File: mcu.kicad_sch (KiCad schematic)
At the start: 47 parts, among them J1 USB_C_Receptacle_USB2.0_16P, J4 Conn_01x03_Pin, J5 Conn_01x03_Pin, J6 Conn_02x04_Odd_Even, J7 AudioJack2_Ground_Switch, SW4 RotaryEncoder_Switch, SW5 RESET, SW6 BOOTSEL, U1 RP2040, U5 W25Q64JVSSIQ, U6 ADS1015IDGS, Y1 XYDBPCNANF-12MHZ

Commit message: stm32g0
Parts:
- removed Brd1: SSD1306, SSD1306:128x64OLED, symbol SSD1306-128x64_OLED:SSD1306
- removed C11, C12: 12pF, Capacitor_SMD:C_0603_1608Metric, symbol Device:C_Small
- removed C13, C14, C15, C16, C17, C19, C20, C26, C5: 0.1uF, Capacitor_SMD:C_0603_1608Metric, symbol Device:C_Small
- removed C18, C21: 1uF, Capacitor_SMD:C_0603_1608Metric, symbol Device:C_Small
- removed J4: Conn_01x03_Pin, Connector_JST:JST_SH_SM03B-SRSS-TB_1x03-1MP_P1.00mm_Horizontal, symbol Connector:Conn_01x03_Pin
- removed J5: Conn_01x03_Pin, Connector_PinHeader_2.54mm:PinHeader_1x03_P2.54mm_Vertical, symbol Connector:Conn_01x03_Pin
- removed J6: Conn_02x04_Odd_Even, Connector_PinHeader_2.54mm:PinHeader_2x04_P2.54mm_Vertical, symbol Connector_Generic:Conn_02x04_Odd_Even
- removed R12, R15, R16, R17: 100K 1%, Resistor_SMD:R_0603_1608Metric, symbol Device:R_Small
- removed R19, R23: 10K, Resistor_SMD:R_0603_1608Metric, symbol Device:R_Small
- removed R20, R21: 22, Resistor_SMD:R_0603_1608Metric, symbol Device:R_Small
- removed R22, R27: 1K, Resistor_SMD:R_0603_1608Metric, symbol Device:R_Small
- removed R47, R48: 100, Resistor_SMD:R_0603_1608Metric, symbol Device:R_US
- removed SW5: RESET, Button_Switch_SMD:SW_Push_1P1T_NO_E-Switch_TL3301NxxxxxG, symbol Switch:SW_Push
- removed SW6: BOOTSEL, Button_Switch_SMD:SW_Push_1P1T_NO_E-Switch_TL3301NxxxxxG, symbol Switch:SW_Push
- removed U1: RP2040, Package_DFN_QFN:QFN-56-1EP_7x7mm_P0.4mm_EP3.2x3.2mm, symbol MCU_RaspberryPi:RP2040
- removed U5: W25Q64JVSSIQ, Package_SO:SOIC-8_5.3x5.3mm_P1.27mm, symbol Memory_Flash_Extra:GD25Q32C
- removed U6: ADS1015IDGS, Package_SO:TSSOP-10_3x3mm_P0.5mm, symbol Analog_ADC:ADS1015IDGS
- removed Y1: XYDBPCNANF-12MHZ, Crystal:Crystal_SMD_3225-4Pin_3.2x2.5mm, symbol Device:Crystal_GND24_Small
- added C28, C37, C39, C47, C48, C49: 100nF, Capacitor_SMD:C_0603_1608Metric, symbol Device:C_Small
- added C29, C30, C42, C43, C44: 4.7uF, Capacitor_SMD:C_0603_1608Metric_Pad1.08x0.95mm_HandSolder, symbol Device:C
- added C45, C46: 100nF, Capacitor_SMD:C_0603_1608Metric, symbol Device:C
- added C50: 1uF, Capacitor_SMD:C_0603_1608Metric, symbol Device:C_Small
- added D15, D16, D17, D18, D19: 1N5819WS, Diode_SMD:D_SOD-323, symbol Diode:1N5819WS
- added D20, D21: SMF18A, Diode_SMD:D_SMF, symbol Diode:SMF18A
- added J2: Conn_01x04_Pin, Connector_PinSocket_2.54mm:PinSocket_1x04_P2.54mm_Vertical, symbol Connector:Conn_01x04_Pin
- added J3: AudioJack2_Ground_Switch, Connector_Audio:Jack_3.5mm_CUI_SJ1-3525N_Horizontal, symbol Connector_Audio:AudioJack3_SwitchTR
- added J4: AudioJack2_Ground_Switch, 2.5mm:Jack_2.5mm_PJ242_6P_12x6.2x4mm_Horizontal, symbol Connector_Audio:AudioJack3_SwitchTR
- added J5, J6: Conn_01x04_Pin, Connector_PinHeader_2.54mm:PinHeader_1x04_P2.54mm_Vertical, symbol Connector:Conn_01x04_Pin
- added Q2: BSS138, Package_TO_SOT_SMD:SOT-23, symbol Transistor_FET:BSS138
- added R29, R30: 22R, Resistor_SMD:R_0603_1608Metric, symbol Device:R_Small
- added R33, R37, R51: 100R, Resistor_SMD:R_0603_1608Metric, symbol Device:R
- added R34, R35: 100K, Resistor_SMD:R_0603_1608Metric_Pad0.98x0.95mm_HandSolder, symbol Device:R
- added R36, R38, R50: 10K, Resistor_SMD:R_0603_1608Metric_Pad0.98x0.95mm_HandSolder, symbol Device:R
- added R39, R43: 680R, Resistor_SMD:R_0603_1608Metric_Pad0.98x0.95mm_HandSolder, symbol Device:R
- added R40, R44: 470K 1%, Resistor_SMD:R_0603_1608Metric, symbol Device:R_Small
- added R41, R45, R46, R47, R48, R49: 100K 1%, Resistor_SMD:R_0603_1608Metric, symbol Device:R_Small
- added R42: 470R, Resistor_SMD:R_0603_1608Metric_Pad0.98x0.95mm_HandSolder, symbol Device:R
- added SW7, SW8, SW9: TRIGGER, Button_Switch_SMD:YZA-032-5.0W, symbol Switch:SW_Push
- added U1: STM32G0B1RETx, Package_QFP:LQFP-64_10x10mm_P0.5mm, symbol MCU_ST_STM32G0:STM32G0B1RETx
- added U8: LM358B, Package_SO:SOIC-8_3.9x4.9mm_P1.27mm, symbol Amplifier_Operational:LM358
- D10, D11, D14, D9: footprint Diode_SMD:D_0201_0603Metric -> Diode_SMD:D_0402_1005Metric; LCSC C52994072 -> C316049
- R10, R9: LCSC (none) -> C23186
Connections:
- net +3.3V: now also C47.1, C48.1, C49.1, C50.1, D15.2 (A), J2.4 (Pin_4), J6.3 (Pin_3), SW9.2, U1.6 (VBAT), U1.7 (VREF+), U1.8 (VDD)
- net +5V: now also R47.1
- net +BATT: now also C28.1, R34.1, R49.1, U8.8 (V+)
- net BATT_SENSE: now also R48.1, R49.2, U1.28 (PB1)
- net BTN_OK: now also U1.54 (PD4)
- net BUZZER1: now also U1.1 (PC11)
- net BUZZER2: now also U1.2 (PC12)
- net CHARGE_PUMP_OSC0: now also R51.1, U1.15 (PC2)
- net CHARGE_PUMP_OSC1: now also R33.1, U1.14 (PC1)
- net CURRENT_SENSE: now also Q2.2 (S), R38.2, R43.2, U1.17 (PA0)
- net D+: now also R30.2
- net D-: now also R29.2
- net GND: now also C28.2, C37.1, C39.1, C44.2, C45.2, C46.2, C47.2, C48.2, C49.2, C50.2, D20.2 (A2), D21.2 (A2), J2.3 (Pin_3), J5.4 (Pin_4), J6.4 (Pin_4), R35.2, R36.1, R41.2, R43.1, R45.2, R46.2, R48.2, SW7.1, SW8.2, U1.9 (VSS), U8.4 (V-)
- net R1: now also SW4.B, U1.53 (PD3); no longer SW4.A
- net R2: now also SW4.A, U1.52 (PD2); no longer SW4.B
- net SWCLK: now also J2.2 (Pin_2), SW9.1, U1.46 (PA14)
- net SWDIO: now also J2.1 (Pin_1), U1.45 (PA13)
- net USB_SENSE: now also R46.1, R47.2, U1.48 (PC8)
- net ~{RESET}: now also C37.2, SW8.1, U1.12 (PF2)
- net FOOT_PEDAL renamed TRIGGER
- net TRIGGER: now also C39.2, SW7.2, U1.29 (PB2)
- new net: R36.2, R50.1, U8.3 (+)
- new net: Q2.1 (G), R39.1
- new net: C43.1, D18.1 (K), D19.2 (A)
- new net: C30.2, C43.2, R51.2
- new net: R34.2, R35.1, U8.5 (+)
- new net: C44.1, D19.1 (K), R37.1
- new net: C29.1, D15.1 (K), D16.2 (A)
- new net: C29.2, C42.2, R33.2
- new net: R38.1, U8.2 (-)
- new net: C30.1, D16.1 (K), D17.2 (A)
- new net: C42.1, D17.1 (K), D18.2 (A)
- new net: R29.1, U1.43 (PA9/PA11)
- new net: R30.1, U1.44 (PA10/PA12)
- new net: R39.2, U8.1
- new net: U8.6 (-), U8.7
- new net: J3.TN, R42.1
- new net BODY_ELECTRODE: D20.1 (A1), J4.R, J4.S, J4.T, R37.2, R44.1
- new net DAC_OUT1: R50.2, U1.21 (PA4)
- new net FOLLICLE_ELECTRODE: D21.1 (A1), J3.R, J3.S, Q2.3 (D), R40.1, R42.2
- new net I2C2_SCL: J6.2 (Pin_2), U1.30 (PB10)
- new net I2C2_SDA: J6.1 (Pin_1), U1.31 (PB11)
- new net OUTPUT_HIGH: C46.1, R44.2, R45.1, U1.32 (PB12)
- new net OUTPUT_LOW: C45.1, R40.2, R41.1, U1.22 (PA5)
- new net PA15: J5.1 (Pin_1), U1.47 (PA15)
- new net PC9: J5.2 (Pin_2), U1.49 (PC9)
- new net PD0: J5.3 (Pin_3), U1.50 (PD0)
- no-connect marks 16 -> 6
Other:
- note added: "Current 0mA-2.426mA w/ 0.6uA stepping"
- note added: "Drive at 1kHz square; alternative phase"
- note added: "Foot pedal can be used or on device button"
- note added: "R for self-testing"
- note removed: "12MHz"
- note removed: "Address 0b1001000"
- note removed: "PWM3 A/B"
- note removed: "PWM7 A/B"
- moved on the sheet: BZ1, C24, D10, D11, D14, D9, J1, J7, R10, R9, SW4

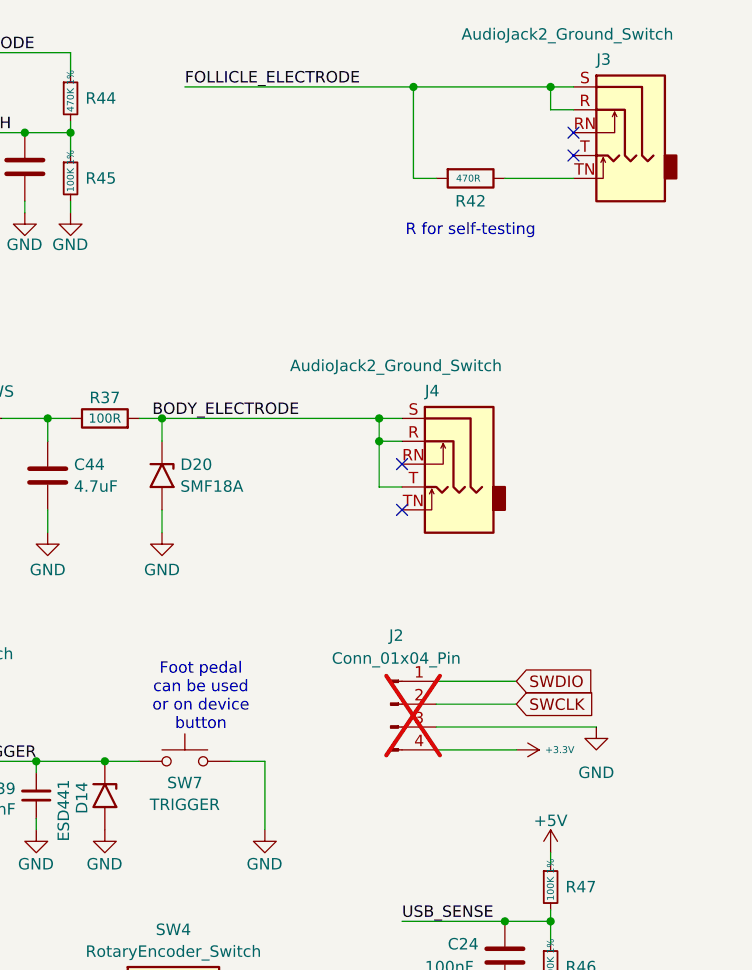
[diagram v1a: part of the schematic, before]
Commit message: fixed some shorts and bad dummy load configuration
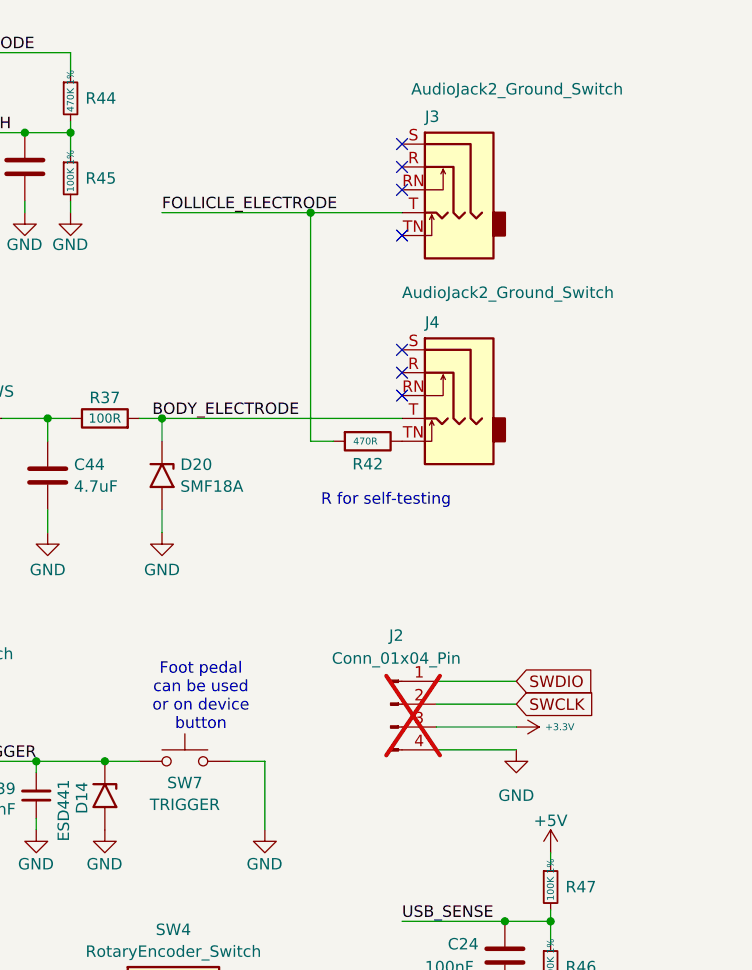
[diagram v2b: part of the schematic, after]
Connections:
- net +3.3V: now also J2.3 (Pin_3); no longer J2.4 (Pin_4)
- net BODY_ELECTRODE: no longer J4.R, J4.S
- net FOLLICLE_ELECTRODE: now also J3.T; no longer J3.R, J3.S
- net GND: now also J2.4 (Pin_4); no longer J2.3 (Pin_3)
- net at J4.TN: now also R42.1
- net at J3.TN: no longer R42.1
- no-connect marks 6 -> 9
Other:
- moved on the sheet: J3, J4, R42

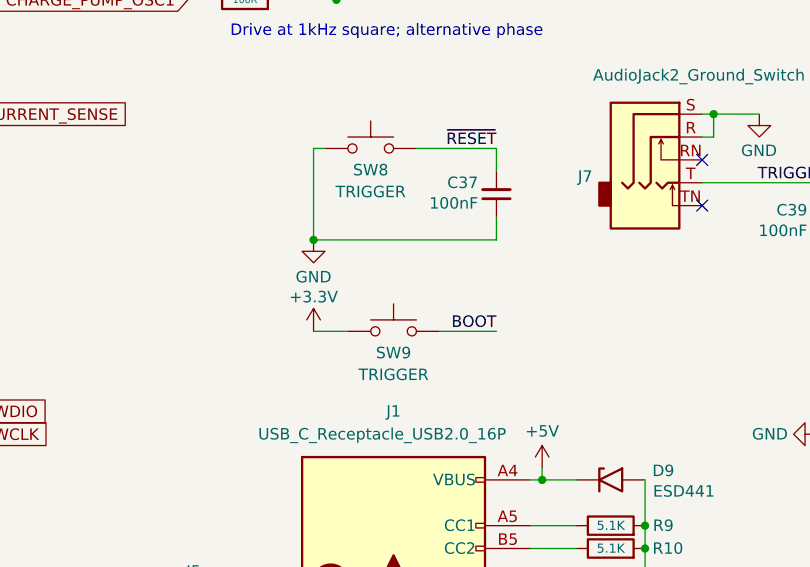
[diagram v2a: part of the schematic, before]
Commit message: Fix C37 LCSC code, changed buttons to C720477
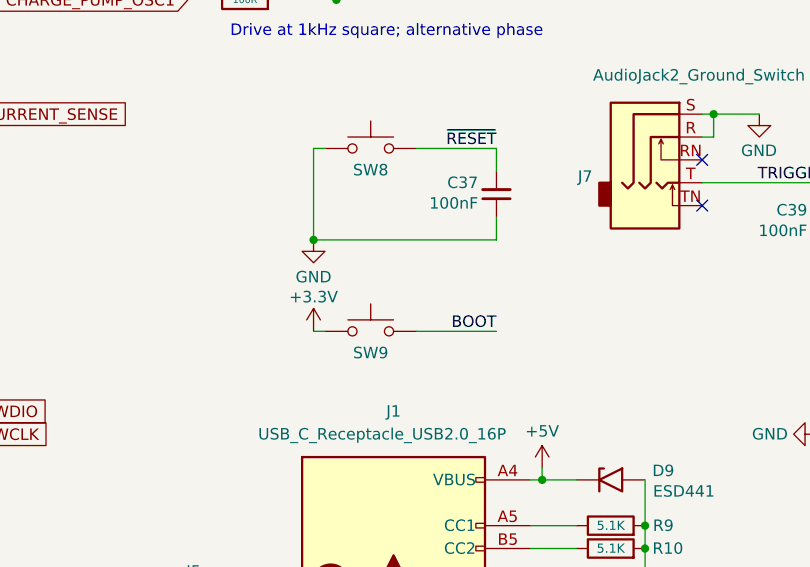
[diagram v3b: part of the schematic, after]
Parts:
- C37: LCSC C15849 -> C14663
- SW8: value TRIGGER -> RST; footprint Button_Switch_SMD:YZA-032-5.0W -> Button_Switch_SMD:SW_SPST_TS-1088-xR025
- SW9: value TRIGGER -> BOOT; footprint Button_Switch_SMD:YZA-032-5.0W -> Button_Switch_SMD:SW_SPST_TS-1088-xR025
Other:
- moved on the sheet: SW9

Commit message: Removed USB resistors, shuffled breakout pins to tidy up a tad
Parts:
- removed R29, R30: 22R, Resistor_SMD:R_0603_1608Metric, symbol Device:R_Small
- SW7: footprint Button_Switch_SMD:YZA-032-5.0W -> Button_Switch_SMD:SW_SPST_TS-1088-xR025; LCSC C49108628 -> C720477
- SW8, SW9: LCSC C49108628 -> C720477
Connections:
- net D+: now also U1.44 (PA10/PA12)
- net D-: now also U1.43 (PA9/PA11)
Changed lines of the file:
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@@
 	(wire
 		(pts
-			(xy 107.95 119.38) (xy 114.3 119.38)
-		)
-		(stroke
-			(width 0)
-			(type default)
-		)
-	)
-	(wire
-		(pts
 			(xy 152.4 60.96) (xy 154.94 60.96)
 		)
@@
 	(wire
 		(pts
-			(xy 99.06 114.3) (xy 102.87 114.3)
+			(xy 99.06 114.3) (xy 114.3 114.3)
 		)
 		(stroke
@@
 	(wire
 		(pts
-			(xy 34.29 101.6) (xy 43.18 101.6)
+			(xy 27.94 101.6) (xy 43.18 101.6)
 		)
 		(stroke
@@
 	(wire
 		(pts
-			(xy 99.06 119.38) (xy 102.87 119.38)
+			(xy 99.06 119.38) (xy 114.3 119.38)
 		)
 		(stroke
@@
 	(wire
 		(pts
-			(xy 107.95 114.3) (xy 114.3 114.3)
-		)
-		(stroke
-			(width 0)
-			(type default)
-		)
-	)
-	(wire
-		(pts
 			(xy 125.73 44.45) (xy 125.73 46.99)
 		)
@@
 	)
 	(label "~{RESET}"
-		(at 34.29 101.6 0)
+		(at 27.94 101.6 0)
 		(effects
 			(font
@@
 			)
 		)
-		(property "LCSC" "C49108628"
+		(property "LCSC" "C720477"
 			(at 158.75 95.25 0)
 			(hide yes)
@@
 			)
 		)
-		(property "Footprint" "Button_Switch_SMD:YZA-032-5.0W"
+		(property "Footprint" "Button_Switch_SMD:SW_SPST_TS-1088-xR025"
 			(at 226.06 93.98 0)
 			(hide yes)
@@
 			)
 		)
-		(property "LCSC" "C49108628"
+		(property "LCSC" "C720477"
 			(at 226.06 99.06 0)
 			(hide yes)
@@
 			)
 		)
-		(property "LCSC" "C49108628"
+		(property "LCSC" "C720477"
 			(at 158.75 115.57 0)
 			(hide yes)
@@
 	(symbol
 		(lib_id "Device:R_Small")
-		(at 105.41 119.38 90)
-		(mirror x)
-		(unit 1)
-		(body_style 1)
-		(exclude_from_sim no)
-		(in_bom yes)
-		(on_board yes)
-		(in_pos_files yes)
-		(dnp no)
-		(property "Reference" "R30"
-			(at 103.378 117.602 90)
-			(show_name no)
-			(do_not_autoplace no)
-			(effects
-				(font
-					(size 1.27 1.27)
-				)
-				(justify right)
-			)
-		)
-		(property "Value" "22R"
-			(at 105.41 119.38 90)
-			(show_name no)
-			(do_not_autoplace no)
-			(effects
-				(font
-					(size 0.762 0.762)
-				)
-			)
-		)
-		(property "Footprint" "Resistor_SMD:R_0603_1608Metric"
-			(at 105.41 119.38 0)
-			(hide yes)
-			(show_name no)
-			(do_not_autoplace no)
-			(effects
-				(font
-					(size 1.27 1.27)
-				)
-			)
-		)
-		(property "Datasheet" ""
-			(at 105.41 119.38 0)
-			(hide yes)
-			(show_name no)
-			(do_not_autoplace no)
-			(effects
-				(font
-					(size 1.27 1.27)
-				)
-			)
-		)
-		(property "Description" "Resistor, small symbol"
-			(at 105.41 119.38 0)
-			(hide yes)
-			(show_name no)
-			(do_not_autoplace no)
-			(effects
-				(font
-					(size 1.27 1.27)
-				)
-			)
-		)
-		(property "LCSC" "C23345"
-			(at 105.41 119.38 90)
-			(hide yes)
-			(show_name no)
-			(do_not_autoplace no)
-			(effects
-				(font
-					(size 1.27 1.27)
-				)
-			)
-		)
-		(pin "1"
-		)
-		(pin "2"
-		)
-		(instances
-			(project "hair-electrolysis-machine"
-				(path "/724ce5ca-e5bf-4553-b755-84be7690a548/cdc4525c-ab23-4870-9f65-db2094403a54"
-					(reference "R30")
-					(unit 1)
-				)
-			)
-		)
-	)
-	(symbol
-		(lib_id "Device:R_Small")
 		(at 266.7 113.03 0)
 		(unit 1)
@@
 					(unit 1)
 				)
-			)
-		)
-	)
-	(symbol
-		(lib_id "Device:R_Small")
-		(at 105.41 114.3 90)
-		(mirror x)
-		(unit 1)
-		(body_style 1)
-		(exclude_from_sim no)
-		(in_bom yes)
-		(on_board yes)
-		(in_pos_files yes)
-		(dnp no)
-		(property "Reference" "R29"
-			(at 103.378 112.522 90)
-			(show_name no)
-			(do_not_autoplace no)
-			(effects
-				(font
-					(size 1.27 1.27)
-				)
-				(justify right)
-			)
-		)
-		(property "Value" "22R"
-			(at 105.41 114.3 90)
-			(show_name no)
-			(do_not_autoplace no)
-			(effects
-				(font
-					(size 0.762 0.762)
-				)
-			)
-		)
-		(property "Footprint" "Resistor_SMD:R_0603_1608Metric"
-			(at 105.41 114.3 0)
-			(hide yes)
-			(show_name no)
-			(do_not_autoplace no)
-			(effects
-				(font
-					(size 1.27 1.27)
-				)
-			)
-		)
-		(property "Datasheet" ""
-			(at 105.41 114.3 0)
-			(hide yes)
-			(show_name no)
-			(do_not_autoplace no)
-			(effects
-				(font
-					(size 1.27 1.27)
-				)
-			)
-		)
-		(property "Description" "Resistor, small symbol"
-			(at 105.41 114.3 0)
-			(hide yes)
-			(show_name no)
-			(do_not_autoplace no)
-			(effects
-				(font
-					(size 1.27 1.27)
-				)
-			)
-		)
-		(property "LCSC" "C23345"
-			(at 105.41 114.3 90)
-			(hide yes)
-			(show_name no)
-			(do_not_autoplace no)
-			(effects
-				(font
-					(size 1.27 1.27)
-				)
-			)
-		)
-		(pin "1"
-		)
-		(pin "2"
-		)
-		(instances
-			(project "hair-electrolysis-machine"
-				(path "/724ce5ca-e5bf-4553-b755-84be7690a548/cdc4525c-ab23-4870-9f65-db2094403a54"
-					(reference "R29")
-					(unit 1)
-				)

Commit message: Use STM32G0B1RBTx, fix up some silkscreen, maybe production ready?
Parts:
- removed U1: STM32G0B1RETx, Package_QFP:LQFP-64_10x10mm_P0.5mm, symbol MCU_ST_STM32G0:STM32G0B1RETx
- added U1: STM32G0B1RBTx, Package_QFP:LQFP-64_10x10mm_P0.5mm, symbol MCU_ST_STM32G0:STM32G0B1RBTx
- C39: LCSC C15849 -> C14663
- J4: LCSC C16684 -> C431536
- J6: footprint Connector_PinHeader_2.54mm:PinHeader_1x04_P2.54mm_Vertical -> Connector_PinSocket_2.54mm:PinSocket_1x04_P2.54mm_Vertical; LCSC (none) -> C2718488
- R34, R35: value 100K -> 100K1%; LCSC C14675 -> C25803
- SW7: value TRIGGER -> BTN
- SW8: value RST -> BTN
- SW9: value BOOT -> BTN
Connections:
- net +3.3V: now also U1.6 (VBAT), U1.7 (VREF+), U1.8 (VDD)
- net BATT_SENSE: now also U1.28 (PB1)
- net BTN_OK: now also U1.54 (PD4)
- net BUZZER1: now also U1.1 (PC11)
- net BUZZER2: now also U1.2 (PC12)
- net CHARGE_PUMP_OSC0: now also U1.15 (PC2)
- net CHARGE_PUMP_OSC1: now also U1.14 (PC1)
- net CURRENT_SENSE: now also U1.17 (PA0)
- net D+: now also U1.44 (PA10/PA12)
- net D-: now also U1.43 (PA9/PA11)
- net DAC_OUT1: now also U1.21 (PA4)
- net GND: now also U1.9 (VSS)
- net I2C2_SCL: now also U1.30 (PB10)
- net I2C2_SDA: now also U1.31 (PB11)
- net OUTPUT_HIGH: now also U1.32 (PB12)
- net OUTPUT_LOW: now also U1.22 (PA5)
- net PA15: now also U1.47 (PA15)
- net PC9: now also U1.49 (PC9)
- net PD0: now also U1.50 (PD0)
- net R1: now also U1.53 (PD3)
- net R2: now also U1.52 (PD2)
- net SWCLK: now also U1.46 (PA14)
- net SWDIO: now also U1.45 (PA13)
- net TRIGGER: now also U1.29 (PB2)
- net USB_SENSE: now also U1.48 (PC8)
- net ~{RESET}: now also U1.12 (PF2)
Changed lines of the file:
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@@
 			)
 		)
-		(property "Value" "RST"
+		(property "Value" "BTN"
 			(at 158.75 100.076 0)
 			(hide yes)
@@
 			)
 		)
-		(property "Value" "100K"
-			(at 49.53 32.004 90)
+		(property "Value" "100K1%"
+			(at 49.53 30.48 90)
 			(show_name no)
 			(do_not_autoplace no)
@@
 					(size 0.762 0.762)
 				)
-				(justify left)
 			)
 		)
@@
 			)
 		)
-		(property "LCSC" "C14675"
+		(property "LCSC" "C25803"
 			(at 49.53 30.48 0)
 			(hide yes)
@@
 			)
 		)
-		(property "Value" "TRIGGER"
+		(property "Value" "BTN"
 			(at 226.06 103.886 0)
 			(show_name no)
@@
 	)
 	(symbol
-		(lib_id "MCU_ST_STM32G0:STM32G0B1RETx")
+		(lib_id "MCU_ST_STM32G0:STM32G0B1RBTx")
 		(at 71.12 132.08 0)
 		(unit 1)
@@
 			)
 		)
-		(property "Value" "STM32G0B1RETx"
+		(property "Value" "STM32G0B1RBTx"
 			(at 73.2633 182.88 0)
 			(show_name no)
@@
 			)
 		)
-		(property "Datasheet" "https://www.st.com/resource/en/datasheet/stm32g0b1re.pdf"
+		(property "Datasheet" "https://www.st.com/resource/en/datasheet/stm32g0b1rb.pdf"
 			(at 71.12 132.08 0)
 			(hide yes)
@@
 			)
 		)
-		(property "Description" "STMicroelectronics Arm Cortex-M0+ MCU, 512KB flash, 144KB RAM, 64 MHz, 1.7-3.6V, 60 GPIO, LQFP64"
+		(property "Description" "STMicroelectronics Arm Cortex-M0+ MCU, 128KB flash, 144KB RAM, 64 MHz, 1.7-3.6V, 60 GPIO, LQFP64"
 			(at 71.12 132.08 0)
 			(hide yes)
@@
 			)
 		)
-		(pin "38"
+		(property "LCSC" "C5143679"
+			(at 71.12 132.08 0)
+			(hide yes)
+			(show_name no)
+			(do_not_autoplace no)
+			(effects
+				(font
+					(size 1.27 1.27)
+				)
+			)
 		)
-		(pin "25"
+		(pin "63"
 		)
-		(pin "26"
+		(pin "64"
 		)
 		(pin "62"
 		)
-		(pin "31"
+		(pin "26"
 		)
-		(pin "33"
+		(pin "25"
 		)
-		(pin "32"
+		(pin "24"
 		)
-		(pin "34"
+		(pin "23"
 		)
-		(pin "35"
+		(pin "22"
 		)
-		(pin "30"
+		(pin "28"
 		)
-		(pin "63"
+		(pin "27"
 		)
-		(pin "39"
+		(pin "30"
 		)
-		(pin "16"
+		(pin "29"
 		)
-		(pin "48"
+		(pin "32"
 		)
-		(pin "50"
+		(pin "31"
 		)
-		(pin "54"
+		(pin "34"
 		)
-		(pin "55"
+		(pin "33"
 		)
-		(pin "53"
+		(pin "37"
 		)
-		(pin "7"
+		(pin "36"
 		)
-		(pin "12"
+		(pin "35"
 		)
-		(pin "11"
+		(pin "44"
 		)
-		(pin "13"
+		(pin "45"
 		)
-		(pin "52"
+		(pin "48"
 		)
-		(pin "14"
+		(pin "49"
 		)
-		(pin "40"
+		(pin "38"
 		)
-		(pin "51"
+		(pin "39"
 		)
-		(pin "56"
+		(pin "40"
 		)
 		(pin "41"
 		)
-		(pin "15"
+		(pin "42"
 		)
-		(pin "10"
+		(pin "43"
 		)
-		(pin "4"
+		(pin "46"
 		)
-		(pin "9"
+		(pin "47"
 		)
-		(pin "2"
+		(pin "50"
 		)
-		(pin "5"
+		(pin "51"
 		)
-		(pin "3"
+		(pin "52"
 		)
-		(pin "64"
+		(pin "53"
 		)
-		(pin "1"
+		(pin "54"
 		)
-		(pin "49"
+		(pin "55"
 		)
-		(pin "8"
+		(pin "56"
 		)
-		(pin "6"
+		(pin "57"
 		)
-		(pin "37"
+		(pin "60"
 		)
-		(pin "44"
+		(pin "61"
 		)
-		(pin "42"
+		(pin "58"
 		)
-		(pin "28"
+		(pin "59"
 		)
-		(pin "45"
+		(pin "1"
 		)
-		(pin "46"
+		(pin "21"
 		)
-		(pin "47"
+		(pin "20"
 		)
-		(pin "27"
+		(pin "19"
 		)
-		(pin "59"
+		(pin "18"
 		)
-		(pin "58"
+		(pin "17"
 		)
-		(pin "60"
+		(pin "16"
 		)
-		(pin "61"
+		(pin "15"
 		)
-		(pin "22"
+		(pin "7"
 		)
-		(pin "23"
+		(pin "8"
 		)
-		(pin "17"
+		(pin "9"
 		)
-		(pin "29"
+		(pin "10"
 		)
-		(pin "57"
+		(pin "14"
 		)
-		(pin "24"
+		(pin "13"
 		)
-		(pin "36"
+		(pin "12"
 		)
-		(pin "43"
+		(pin "11"
 		)
-		(pin "21"
+		(pin "2"
 		)
-		(pin "20"
+		(pin "3"
 		)
-		(pin "19"
+		(pin "4"
 		)
-		(pin "18"
+		(pin "5"
+		)
+		(pin "6"
 		)
 		(instances
@@
 			)
 		)
-		(property "LCSC" "C16684"
+		(property "LCSC" "C431536"
 			(at 255.27 55.88 0)
 			(hide yes)
@@
 			)
 		)
-		(property "Value" "BOOT"
+		(property "Value" "BTN"
 			(at 158.75 120.396 0)
 			(hide yes)
@@
 			)
 		)
-		(property "LCSC" "C15849"
+		(property "LCSC" "C14663"
 			(at 209.55 102.87 90)
 			(hide yes)
@@
 			)
 		)
-		(property "Value" "100K"
-			(at 49.53 44.704 90)
+		(property "Value" "100K1%"
+			(at 49.53 43.18 90)
 			(show_name no)
 			(do_not_autoplace no)
@@
 					(size 0.762 0.762)
 				)
-				(justify left)
 			)
 		)
@@
 			)
 		)
-		(property "LCSC" "C14675"
+		(property "LCSC" "C25803"
 			(at 49.53 43.18 0)
 			(hide yes)
@@
 			)
 		)
-		(property "Footprint" "Connector_PinHeader_2.54mm:PinHeader_1x04_P2.54mm_Vertical"
+		(property "Footprint" "Connector_PinSocket_2.54mm:PinSocket_1x04_P2.54mm_Vertical"
 			(at 224.79 151.13 0)
 			(hide yes)
@@
 			(at 224.79 151.13 0)
 			(hide yes)
+			(show_name no)
+			(do_not_autoplace no)
+			(effects
+				(font
+					(size 1.27 1.27)
+				)
+			)
+		)
+		(property "LCSC" "C2718488"
+			(at 224.79 151.13 0)
+			(hide yes)
